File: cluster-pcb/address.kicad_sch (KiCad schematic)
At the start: 13 parts, among them SW1201 SW_DIP_x08_SDA08H1SBDR, U1201 TCA6408ARGTR

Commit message: Update schematic
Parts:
- renumbered R1209 to R1201, R1201 to R1202, R1202 to R1203, R1203 to R1204, R1204 to R1205, R1205 to R1206, R1206 to R1207, R1207 to R1208, R1208 to R1209
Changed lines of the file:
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@@
   (title_block
     (title "cluster-pcb")
-    (date "2024-09-10")
+    (date "2024-09-12")
     (rev "1.2")
     (company "Howard Hughes Medical Institute")
@@
   (symbol (lib_id "Janelia:R_10.0k_0402") (at 128.27 128.27 0) (unit 1)
     (in_bom yes) (on_board yes) (dnp no)
-    (property "Reference" "R1202" (at 129.54 128.27 0)
+    (property "Reference" "R1203" (at 129.54 128.27 0)
       (effects (font (size 1.016 1.016)) (justify left))
     )
@@
       (project "cluster-pcb"
         (path "/df2b2e89-e055-4140-95de-f1df723db034/4efcb6a8-711f-428b-9f4e-1f72ad1e6234"
-          (reference "R1202") (unit 1)
+          (reference "R1203") (unit 1)
         )
       )
@@
   (symbol (lib_id "Janelia:R_10.0k_0402") (at 55.88 90.17 0) (unit 1)
     (in_bom yes) (on_board yes) (dnp no)
-    (property "Reference" "R1209" (at 57.15 90.17 0)
+    (property "Reference" "R1201" (at 57.15 90.17 0)
       (effects (font (size 1.016 1.016)) (justify left))
     )
@@
       (project "cluster-pcb"
         (path "/df2b2e89-e055-4140-95de-f1df723db034/4efcb6a8-711f-428b-9f4e-1f72ad1e6234"
-          (reference "R1209") (unit 1)
+          (reference "R1201") (unit 1)
         )
       )
@@
   (symbol (lib_id "Janelia:R_10.0k_0402") (at 172.72 128.27 0) (unit 1)
     (in_bom yes) (on_board yes) (dnp no)
-    (property "Reference" "R1207" (at 173.99 128.27 0)
+    (property "Reference" "R1208" (at 173.99 128.27 0)
       (effects (font (size 1.016 1.016)) (justify left))
     )
@@
       (project "cluster-pcb"
         (path "/df2b2e89-e055-4140-95de-f1df723db034/4efcb6a8-711f-428b-9f4e-1f72ad1e6234"
-          (reference "R1207") (unit 1)
+          (reference "R1208") (unit 1)
         )
       )
@@
   (symbol (lib_id "Janelia:R_10.0k_0402") (at 137.16 128.27 0) (unit 1)
     (in_bom yes) (on_board yes) (dnp no)
-    (property "Reference" "R1203" (at 138.43 128.27 0)
+    (property "Reference" "R1204" (at 138.43 128.27 0)
       (effects (font (size 1.016 1.016)) (justify left))
     )
@@
       (project "cluster-pcb"
         (path "/df2b2e89-e055-4140-95de-f1df723db034/4efcb6a8-711f-428b-9f4e-1f72ad1e6234"
-          (reference "R1203") (unit 1)
+          (reference "R1204") (unit 1)
         )
       )
@@
   (symbol (lib_id "Janelia:R_10.0k_0402") (at 154.94 128.27 0) (unit 1)
     (in_bom yes) (on_board yes) (dnp no)
-    (property "Reference" "R1205" (at 156.21 128.27 0)
+    (property "Reference" "R1206" (at 156.21 128.27 0)
       (effects (font (size 1.016 1.016)) (justify left))
     )
@@
       (project "cluster-pcb"
         (path "/df2b2e89-e055-4140-95de-f1df723db034/4efcb6a8-711f-428b-9f4e-1f72ad1e6234"
-          (reference "R1205") (unit 1)
+          (reference "R1206") (unit 1)
         )
       )
@@
   (symbol (lib_id "Janelia:R_10.0k_0402") (at 181.61 128.27 0) (unit 1)
     (in_bom yes) (on_board yes) (dnp no)
-    (property "Reference" "R1208" (at 182.88 128.27 0)
+    (property "Reference" "R1209" (at 182.88 128.27 0)
       (effects (font (size 1.016 1.016)) (justify left))
     )
@@
       (project "cluster-pcb"
         (path "/df2b2e89-e055-4140-95de-f1df723db034/4efcb6a8-711f-428b-9f4e-1f72ad1e6234"
-          (reference "R1208") (unit 1)
+          (reference "R1209") (unit 1)
         )
       )
@@
   (symbol (lib_id "Janelia:R_10.0k_0402") (at 146.05 128.27 0) (unit 1)
     (in_bom yes) (on_board yes) (dnp no)
-    (property "Reference" "R1204" (at 147.32 128.27 0)
+    (property "Reference" "R1205" (at 147.32 128.27 0)
       (effects (font (size 1.016 1.016)) (justify left))
     )
@@
       (project "cluster-pcb"
         (path "/df2b2e89-e055-4140-95de-f1df723db034/4efcb6a8-711f-428b-9f4e-1f72ad1e6234"
-          (reference "R1204") (unit 1)
+          (reference "R1205") (unit 1)
         )
       )
@@
   (symbol (lib_id "Janelia:R_10.0k_0402") (at 163.83 128.27 0) (unit 1)
     (in_bom yes) (on_board yes) (dnp no)
-    (property "Reference" "R1206" (at 165.1 128.27 0)
+    (property "Reference" "R1207" (at 165.1 128.27 0)
       (effects (font (size 1.016 1.016)) (justify left))
     )
@@
       (project "cluster-pcb"
         (path "/df2b2e89-e055-4140-95de-f1df723db034/4efcb6a8-711f-428b-9f4e-1f72ad1e6234"
-          (reference "R1206") (unit 1)
+          (reference "R1207") (unit 1)
         )
       )
@@
   (symbol (lib_id "Janelia:R_10.0k_0402") (at 119.38 128.27 0) (unit 1)
     (in_bom yes) (on_board yes) (dnp no)
-    (property "Reference" "R1201" (at 120.65 128.27 0)
+    (property "Reference" "R1202" (at 120.65 128.27 0)
       (effects (font (size 1.016 1.016)) (justify left))
     )
@@
       (project "cluster-pcb"
         (path "/df2b2e89-e055-4140-95de-f1df723db034/4efcb6a8-711f-428b-9f4e-1f72ad1e6234"
-          (reference "R1201") (unit 1)
-        )
-      )
+          (reference "R1202") (unit 1)
+        )
+      )

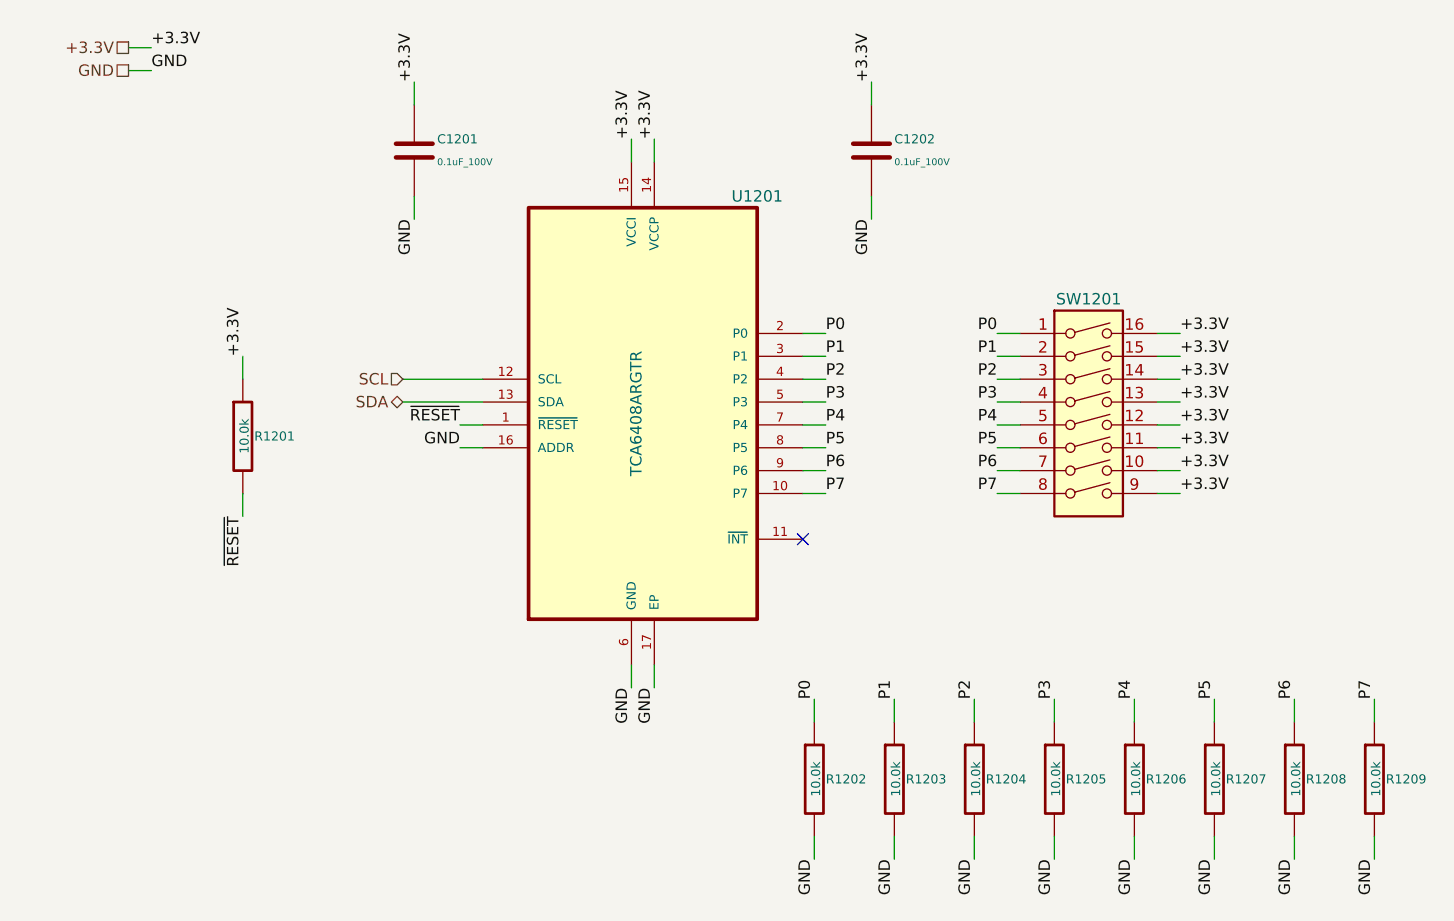
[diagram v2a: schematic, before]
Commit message: Fix ERC issues
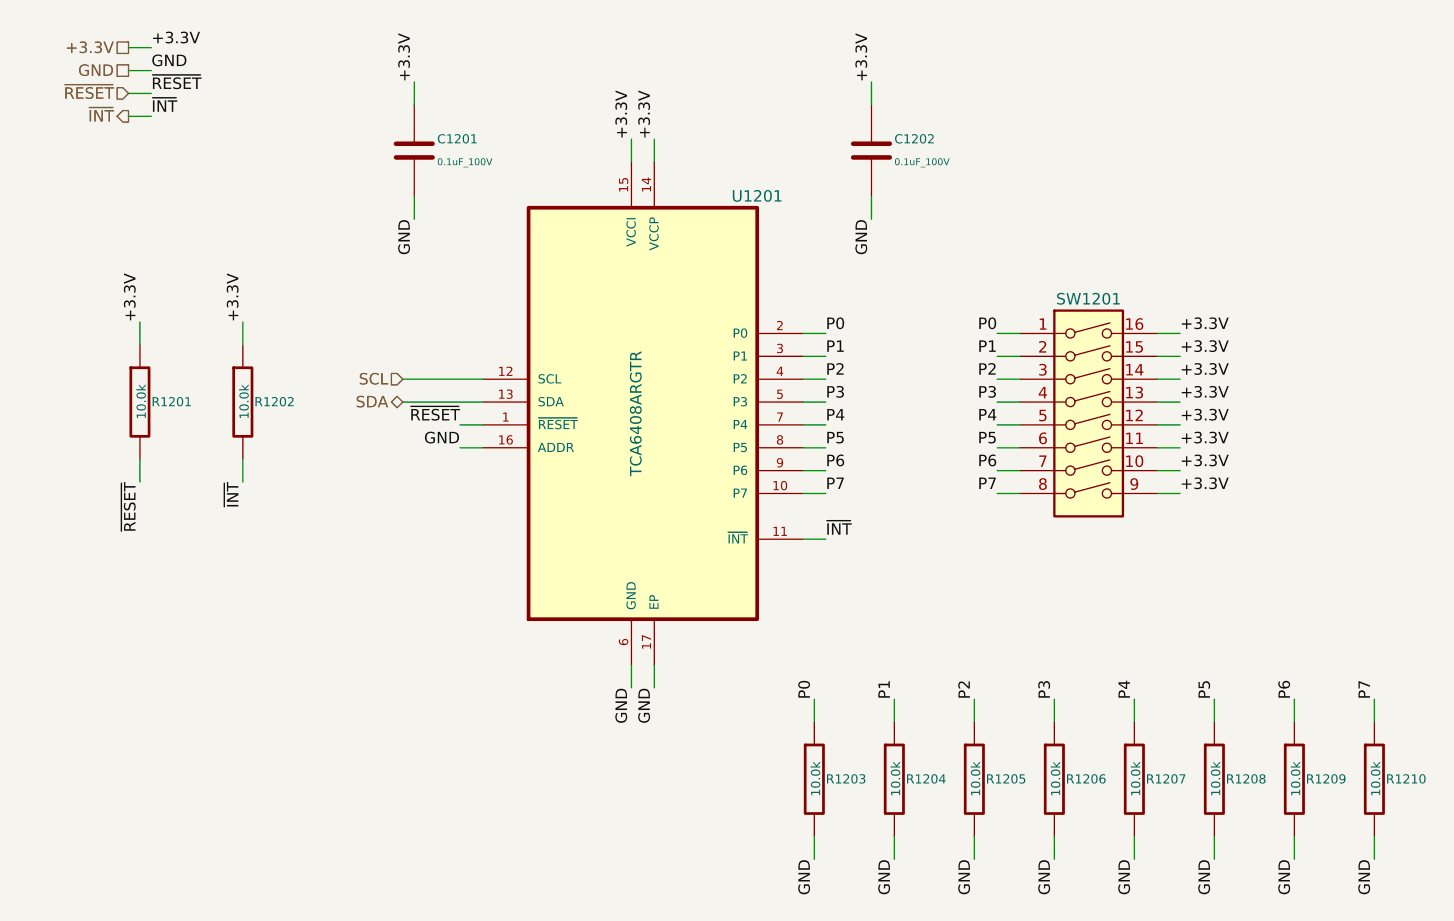
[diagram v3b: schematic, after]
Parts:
- added R1202: 10.0k, Janelia:R_0402_1005Metric, symbol Janelia:R_10.0k_0402
- renumbered R1202 to R1203, R1203 to R1204, R1204 to R1205, R1205 to R1206, R1206 to R1207, R1207 to R1208, R1208 to R1209, R1209 to R1210
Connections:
- net +3.3V: now also R1202.1
- net ~{INT}: now reaches U1201.11 (~{INT})
- net ~{INT}: now also R1202.2
- no-connect marks 1 -> 0
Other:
- moved on the sheet: R1201
